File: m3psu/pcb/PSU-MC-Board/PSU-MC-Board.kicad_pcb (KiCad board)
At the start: 2 copper layers, 40 x 40 mm, 56 parts, among them IC1 STM32F405RxTx, IC2 TPS62152, IC3 MCP2562, IC4 LTC4353, IC5 LTC4151, J1 WEST TOP, J2 WEST BOT, J3 NORTH TOP, J4 EAST TOP, J5 EAST BOT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

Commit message: Finished routing PSU uC board. Just needs checking.
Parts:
- moved Q8 9.24 mm to (115.1, 110.2)
- moved R8 8.08 mm to (102.8, 88.6), turned to 180 degrees
- moved R11 7.96 mm to (98.8, 102.0)
- moved R16 6.77 mm to (112.7, 113.0), turned to 180 degrees
- moved Q3 5.87 mm to (107.3, 97.5), turned to 0 degrees
- moved C15 5.68 mm to (93.7, 97.2), turned to 0 degrees
- moved Q7 5.38 mm to (105.8, 99.1)
- moved Q6 5.23 mm to (107.8, 96.0)
- moved C17 4.96 mm to (93.5, 98.6), turned to 0 degrees
- moved R10 4.88 mm to (104.7, 89.4), turned to 90 degrees
- moved R12 4.31 mm to (109.1, 99.4), turned to 180 degrees
- moved R14 3.82 mm to (105.9, 96.5), turned to 270 degrees
- moved R15 3.19 mm to (111.7, 110.6), turned to 270 degrees
- moved Q9 3.12 mm to (107.7, 114.1)
- moved IC4 2.44 mm to (92.1, 94.8), turned to 270 degrees
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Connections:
- IC1 pad 16: Net-(IC1-Pad16) -> /EN_PYRO
- IC1 pad 24: Net-(IC1-Pad24) -> /BLEED_BATT2
- IC1 pad 25: Net-(IC1-Pad25) -> /BLEED_BATT1
- IC1 pad 39: Net-(IC1-Pad39) -> /~EN_INT_PWR
- IC1 pad 43: Net-(IC1-Pad43) -> /~EN_EXT_PWR
- IC1 pad 44: Net-(IC1-Pad44) -> /~EXT_PWR_ON
- IC1 pad 45: Net-(IC1-Pad45) -> /~INT_PWR_ON
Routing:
- net VCC: track 34.6 -> 67.2 mm, vias 4 -> 7
- net /PYRO1: track 0.00 -> 32.2 mm, vias 0 -> 4
- net /PWR: track 2.73 -> 33.6 mm, vias 0 -> 4
- net GND: track 50.3 -> 80.1 mm, vias 11 -> 26
- net 3v3: track 75.1 -> 100.5 mm, vias 5 -> 12
- net /BATT2: track 3.28 -> 24.3 mm, vias 1 -> 4
- net /BATT1: track 3.28 -> 22.2 mm, vias 1 -> 5
- net /SDA: track 27.4 -> 46.1 mm
- net /BLEED_BATT2: track 0.00 -> 14.8 mm, vias 0 -> 2
- net /~INT_PWR_ON: track 0.00 -> 13.3 mm
- net /~EN_INT_PWR: track 0.51 -> 13.0 mm, vias 0 -> 2
- net /BLEED_BATT1: track 0.00 -> 12.1 mm, vias 0 -> 2
- net /SCL: track 31.9 -> 43.0 mm
- net /~EXT_PWR_ON: track 0.00 -> 10.4 mm
- net Net-(Q8-PadG): track 0.00 -> 10.3 mm
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
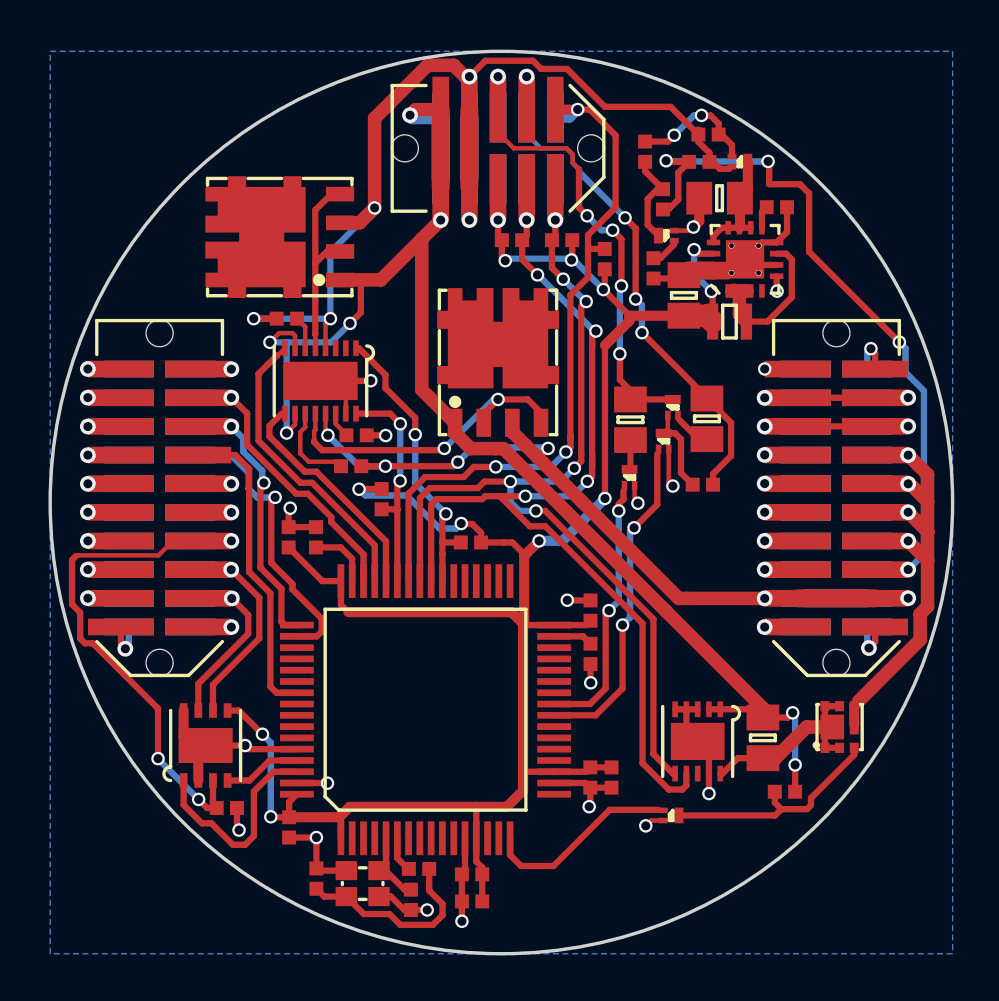
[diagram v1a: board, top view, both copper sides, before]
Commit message: Finished routing the Li-ion Charger board. Needs checking. Did a brief check of the MCU board. Not done yet.
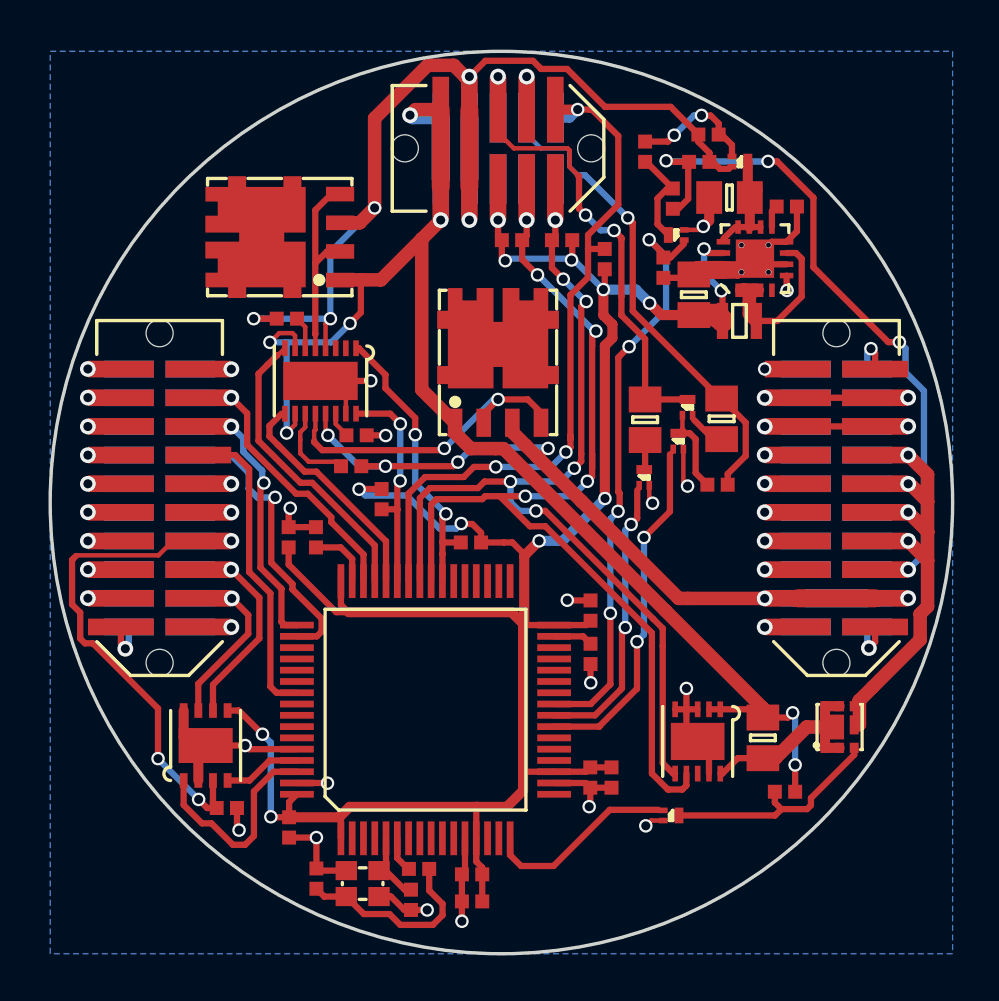
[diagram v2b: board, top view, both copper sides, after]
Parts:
- moved Q6 0.65 mm to (108.4, 96.0)
- moved Q7 0.65 mm to (106.5, 99.1)
- moved R12 0.65 mm to (109.7, 99.4)
- moved Q3 0.65 mm to (108.0, 97.5)
- moved R13 0.65 mm to (109.9, 96.5)
- moved R14 0.65 mm to (106.5, 96.5)
- moved C14 0.44 mm to (108.7, 91.0)
- moved Q1 0.44 mm to (107.9, 88.3)
- moved C12 0.44 mm to (110.3, 86.7)
- moved C13 0.44 mm to (112.8, 87.1)
- moved IC2 0.44 mm to (111.4, 89.4)
- moved L1 0.44 mm to (110.7, 92.2)
- moved R4 0.44 mm to (107.8, 86.7)
- moved R2 0.44 mm to (107.3, 89.8)
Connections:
- IC1 pad 23: Net-(IC1-Pad23) -> /BLEED_BATT2
- IC1 pad 24: /BLEED_BATT2 -> /BLEED_BATT1
- IC1 pad 25: /BLEED_BATT1 -> /~SHUTDOWN
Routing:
- net /~SHUTDOWN: track 1.34 -> 26.4 mm, vias 0 -> 4
- net 3v3: track 100.5 -> 103.2 mm, vias 12 -> 13
- net /BLEED_BATT2: track 14.8 -> 15.8 mm
- net Net-(IC5-Pad10): track 9.23 -> 10.2 mm
- net /BATT2: track 24.3 -> 25.1 mm, vias 4 -> 2
- net /BLEED_BATT1: track 12.1 -> 12.8 mm
- net /BATT1: track 22.2 -> 22.8 mm, vias 5 -> 3

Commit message: Added on the battery voltage monitoring.
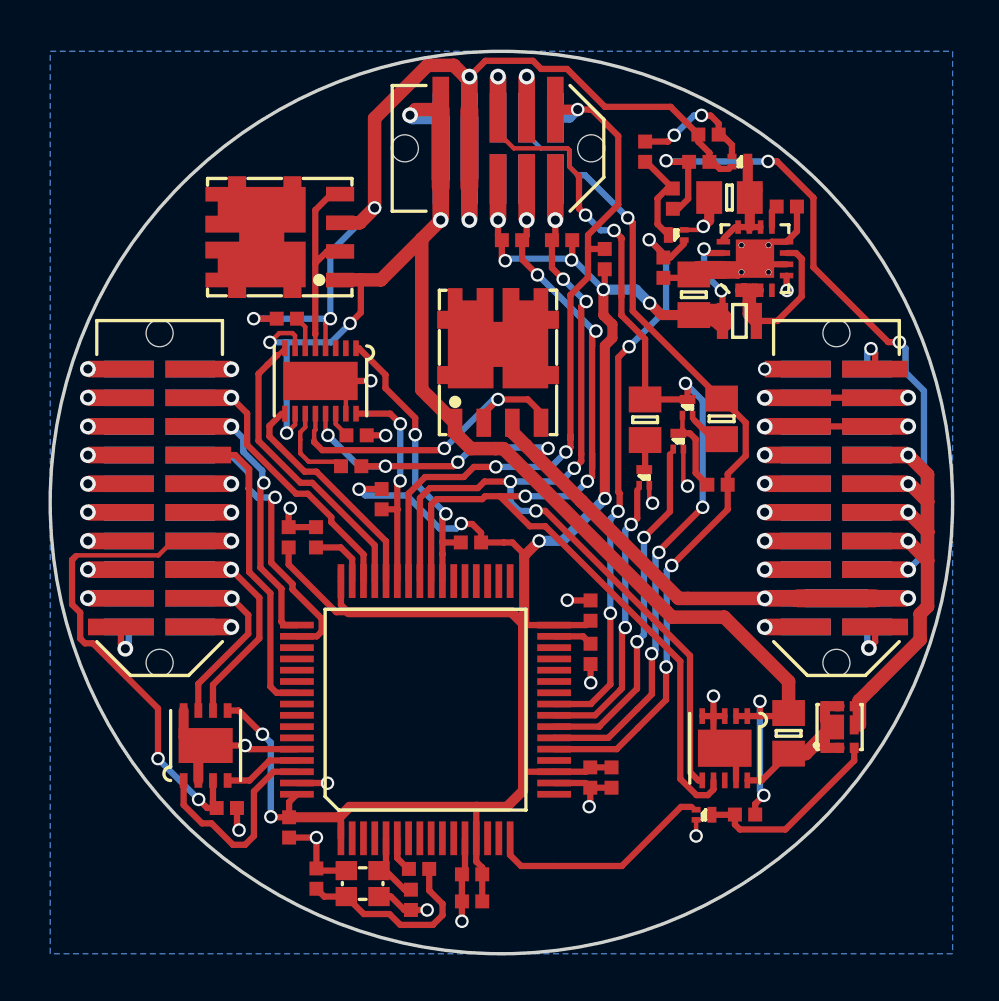
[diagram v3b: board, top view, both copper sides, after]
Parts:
- moved R16 2.04 mm to (111.0, 114.0)
- moved Q9 1.46 mm to (109.1, 114.0)
- moved IC5 1.24 mm to (110.0, 111.1)
- moved R15 1.16 mm to (112.9, 110.4)
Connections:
- IC1 pad 10: Net-(IC1-Pad10) -> (no net)
- IC1 pad 11: Net-(IC1-Pad11) -> (no net)
- IC1 pad 14: Net-(IC1-Pad14) -> (no net)
- IC1 pad 15: Net-(IC1-Pad15) -> (no net)
- IC1 pad 17: Net-(IC1-Pad17) -> (no net)
- IC1 pad 2: Net-(IC1-Pad2) -> (no net)
- IC1 pad 20: Net-(IC1-Pad20) -> (no net)
- IC1 pad 21: Net-(IC1-Pad21) -> /BATT2
- IC1 pad 22: Net-(IC1-Pad22) -> /BATT1
- IC1 pad 26: Net-(IC1-Pad26) -> (no net)
- IC1 pad 27: Net-(IC1-Pad27) -> (no net)
- IC1 pad 28: Net-(IC1-Pad28) -> (no net)
- IC1 pad 29: Net-(IC1-Pad29) -> (no net)
- IC1 pad 3: Net-(IC1-Pad3) -> (no net)
- IC1 pad 30: Net-(IC1-Pad30) -> (no net)
- IC1 pad 33: Net-(IC1-Pad33) -> (no net)
- IC1 pad 34: Net-(IC1-Pad34) -> (no net)
- IC1 pad 35: Net-(IC1-Pad35) -> (no net)
- IC1 pad 36: Net-(IC1-Pad36) -> (no net)
- IC1 pad 37: Net-(IC1-Pad37) -> (no net)
- IC1 pad 38: Net-(IC1-Pad38) -> (no net)
- IC1 pad 4: Net-(IC1-Pad4) -> (no net)
- IC1 pad 51: Net-(IC1-Pad51) -> (no net)
- IC1 pad 52: Net-(IC1-Pad52) -> (no net)
- IC1 pad 53: Net-(IC1-Pad53) -> (no net)
- IC1 pad 54: Net-(IC1-Pad54) -> (no net)
- IC1 pad 56: Net-(IC1-Pad56) -> (no net)
- IC1 pad 57: Net-(IC1-Pad57) -> (no net)
- IC1 pad 58: Net-(IC1-Pad58) -> (no net)
- IC1 pad 59: Net-(IC1-Pad59) -> (no net)
- IC1 pad 7: Net-(IC1-Pad7) -> (no net)
- IC1 pad 8: Net-(IC1-Pad8) -> (no net)
- IC1 pad 9: Net-(IC1-Pad9) -> (no net)
- IC2 pad 4: Net-(IC2-Pad4) -> (no net)
- IC4 pad 2: Net-(IC4-Pad2) -> (no net)
- IC4 pad 3: Net-(IC4-Pad3) -> (no net)
- IC5 pad 8: Net-(IC5-Pad8) -> (no net)
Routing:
- net /BATT1: track 22.8 -> 43.8 mm, vias 3 -> 7
- net /BATT2: track 25.1 -> 41.7 mm, vias 2 -> 4
- net VCC: track 67.2 -> 69.2 mm
- net /EN_PYRO: track 8.77 -> 10.6 mm
- net Net-(Q8-PadG): track 10.3 -> 8.68 mm
- net Net-(IC5-Pad10): track 10.2 -> 9.16 mm
- net /SCL: track 43.0 -> 43.8 mm
- net /SDA: track 46.1 -> 46.8 mm

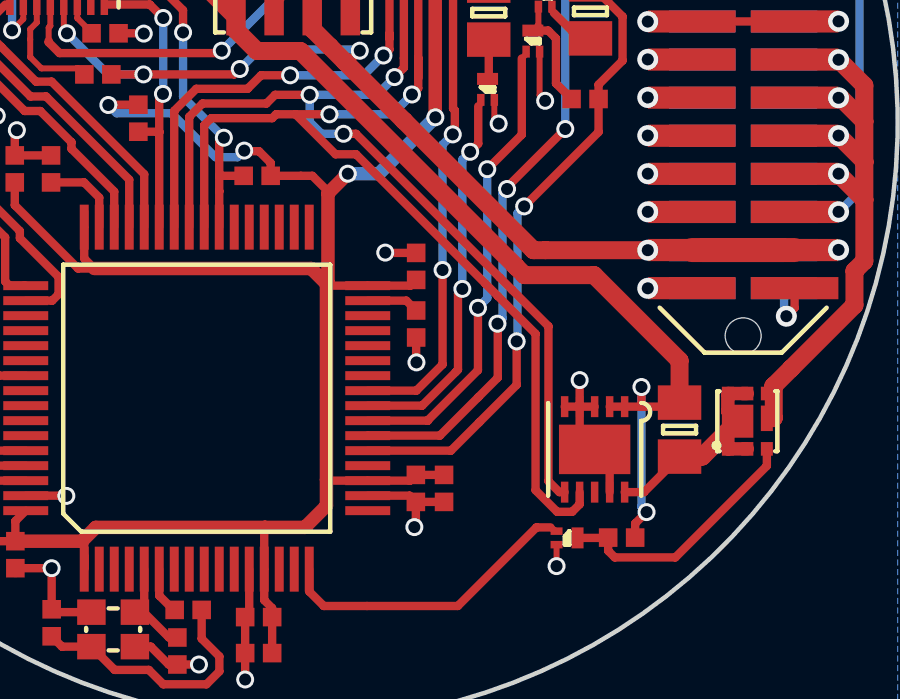
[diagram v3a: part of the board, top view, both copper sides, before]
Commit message: Add voltage dividers to battery monitor lines
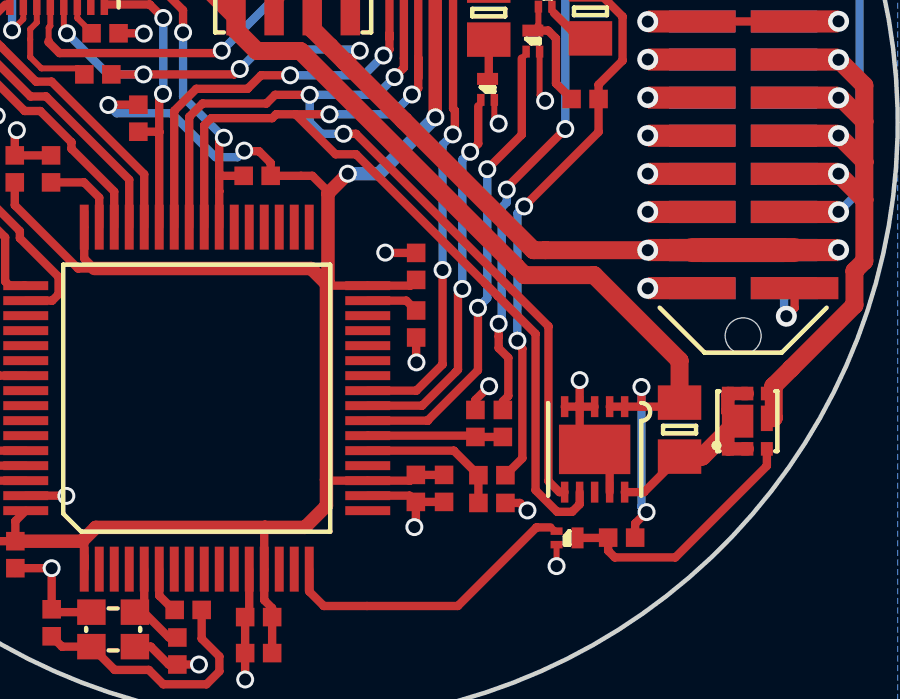
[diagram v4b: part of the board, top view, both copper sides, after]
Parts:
- added R17: 30k, agg:0402, F.Cu at (106.6, 112.0)
- added R18: 10k, agg:0402, F.Cu at (106.6, 112.9)
- added R19: 10k, agg:0402, F.Cu at (107.0, 110.2)
- added R20: 10k, agg:0402, F.Cu at (106.1, 110.2)
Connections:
- IC1 pad 10: (no net) -> Net-(IC1-Pad10)
- IC1 pad 11: (no net) -> Net-(IC1-Pad11)
- IC1 pad 14: (no net) -> Net-(IC1-Pad14)
- IC1 pad 15: (no net) -> Net-(IC1-Pad15)
- IC1 pad 17: (no net) -> Net-(IC1-Pad17)
- IC1 pad 2: (no net) -> Net-(IC1-Pad2)
- IC1 pad 20: (no net) -> Net-(IC1-Pad20)
- IC1 pad 21: /BATT2 -> /BATT2_MONITOR
- IC1 pad 22: /BATT1 -> /BATT1_MONITOR
- IC1 pad 26: (no net) -> Net-(IC1-Pad26)
- IC1 pad 27: (no net) -> Net-(IC1-Pad27)
- IC1 pad 28: (no net) -> Net-(IC1-Pad28)
- IC1 pad 29: (no net) -> Net-(IC1-Pad29)
- IC1 pad 3: (no net) -> Net-(IC1-Pad3)
- IC1 pad 30: (no net) -> Net-(IC1-Pad30)
- IC1 pad 33: (no net) -> Net-(IC1-Pad33)
- IC1 pad 34: (no net) -> Net-(IC1-Pad34)
- IC1 pad 35: (no net) -> Net-(IC1-Pad35)
- IC1 pad 36: (no net) -> Net-(IC1-Pad36)
- IC1 pad 37: (no net) -> Net-(IC1-Pad37)
- IC1 pad 38: (no net) -> Net-(IC1-Pad38)
- IC1 pad 4: (no net) -> Net-(IC1-Pad4)
- IC1 pad 51: (no net) -> Net-(IC1-Pad51)
- IC1 pad 52: (no net) -> Net-(IC1-Pad52)
- IC1 pad 53: (no net) -> Net-(IC1-Pad53)
- IC1 pad 54: (no net) -> Net-(IC1-Pad54)
- IC1 pad 56: (no net) -> Net-(IC1-Pad56)
- IC1 pad 57: (no net) -> Net-(IC1-Pad57)
- IC1 pad 58: (no net) -> Net-(IC1-Pad58)
- IC1 pad 59: (no net) -> Net-(IC1-Pad59)
- IC1 pad 7: (no net) -> Net-(IC1-Pad7)
- IC1 pad 8: (no net) -> Net-(IC1-Pad8)
- IC1 pad 9: (no net) -> Net-(IC1-Pad9)
- IC2 pad 4: (no net) -> Net-(IC2-Pad4)
- IC4 pad 2: (no net) -> Net-(IC4-Pad2)
- IC4 pad 3: (no net) -> Net-(IC4-Pad3)
- IC5 pad 8: (no net) -> Net-(IC5-Pad8)
- Q1 pad D: Net-(Q1-PadD) -> (no net)
- Q1 pad G: /~SHUTDOWN -> (no net)
- Q1 pad S: GND -> (no net)
- Q2 pad D: Net-(C12-Pad1) -> (no net)
- Q2 pad G: Net-(Q2-PadG) -> (no net)
- Q2 pad S: VBATT -> (no net)
- Q3 pad D: Net-(Q3-PadD) -> (no net)
- Q3 pad G: /BLEED_BATT2 -> (no net)
- Q3 pad S: GND -> (no net)
- Q6 pad D: /BATT1 -> (no net)
- Q6 pad G: Net-(Q3-PadD) -> (no net)
- Q6 pad S: Net-(Q6-PadS) -> (no net)
- Q7 pad D: Net-(Q7-PadD) -> (no net)
- Q7 pad G: /BLEED_BATT1 -> (no net)
- Q7 pad S: GND -> (no net)
- Q8 pad D: /PYRO1 -> (no net)
- Q8 pad G: Net-(Q8-PadG) -> (no net)
- Q8 pad S: Net-(IC5-Pad10) -> (no net)
- Q9 pad D: Net-(Q8-PadG) -> (no net)
- Q9 pad G: /EN_PYRO -> (no net)
- Q9 pad S: GND -> (no net)
- R12 pad 2: Net-(Q3-PadD) -> Net-(Q3-Pad3)
- R13 pad 2: Net-(Q6-PadS) -> Net-(Q6-Pad2)
- R14 pad 2: Net-(Q7-PadD) -> Net-(Q7-Pad3)
- R16 pad 2: Net-(Q8-PadG) -> Net-(Q8-Pad1)
- R4 pad 2: Net-(Q1-PadD) -> Net-(Q1-Pad3)
- R5 pad 2: Net-(Q2-PadG) -> Net-(Q2-Pad1)
- R6 pad 1: Net-(Q2-PadG) -> Net-(Q2-Pad1)
- R6 pad 2: Net-(Q1-PadD) -> Net-(Q1-Pad3)
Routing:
- net Net-(Q8-PadG): track 8.68 -> 0.00 mm
- net Net-(Q8-Pad1): track 0.00 -> 8.68 mm
- net Net-(Q2-PadG): track 5.68 -> 0.00 mm, vias 2 -> 0
- net Net-(Q2-Pad1): track 0.00 -> 5.68 mm, vias 0 -> 2
- net /BATT2_MONITOR: track 0.00 -> 4.95 mm
- net /BATT1_MONITOR: track 0.00 -> 4.52 mm
- net Net-(Q1-PadD): track 4.48 -> 0.00 mm
- net Net-(Q1-Pad3): track 0.00 -> 4.48 mm
- net Net-(Q3-PadD): track 3.99 -> 0.00 mm
- net Net-(Q3-Pad3): track 0.00 -> 3.99 mm
- net /BATT1: track 43.8 -> 39.9 mm
- net (no net): track 0.00 -> 3.28 mm, vias 0 -> 3
- net /BATT2: track 41.7 -> 39.1 mm
- net Net-(Q6-PadS): track 1.81 -> 0.00 mm
- net Net-(Q6-Pad2): track 0.00 -> 1.81 mm
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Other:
- rule pad_to_mask_clearance: 0.2 -> 0
